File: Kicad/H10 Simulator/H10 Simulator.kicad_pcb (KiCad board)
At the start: 4 copper layers, 54 x 35.2 mm, 15 parts, among them J1 To Controller, J2 H10 ReaderPunch, J3 To Simulator, U1 74xx165, U2 74xx595, U3 74xx04, U4 74xx595, U5 74xx165, U6 74xx04

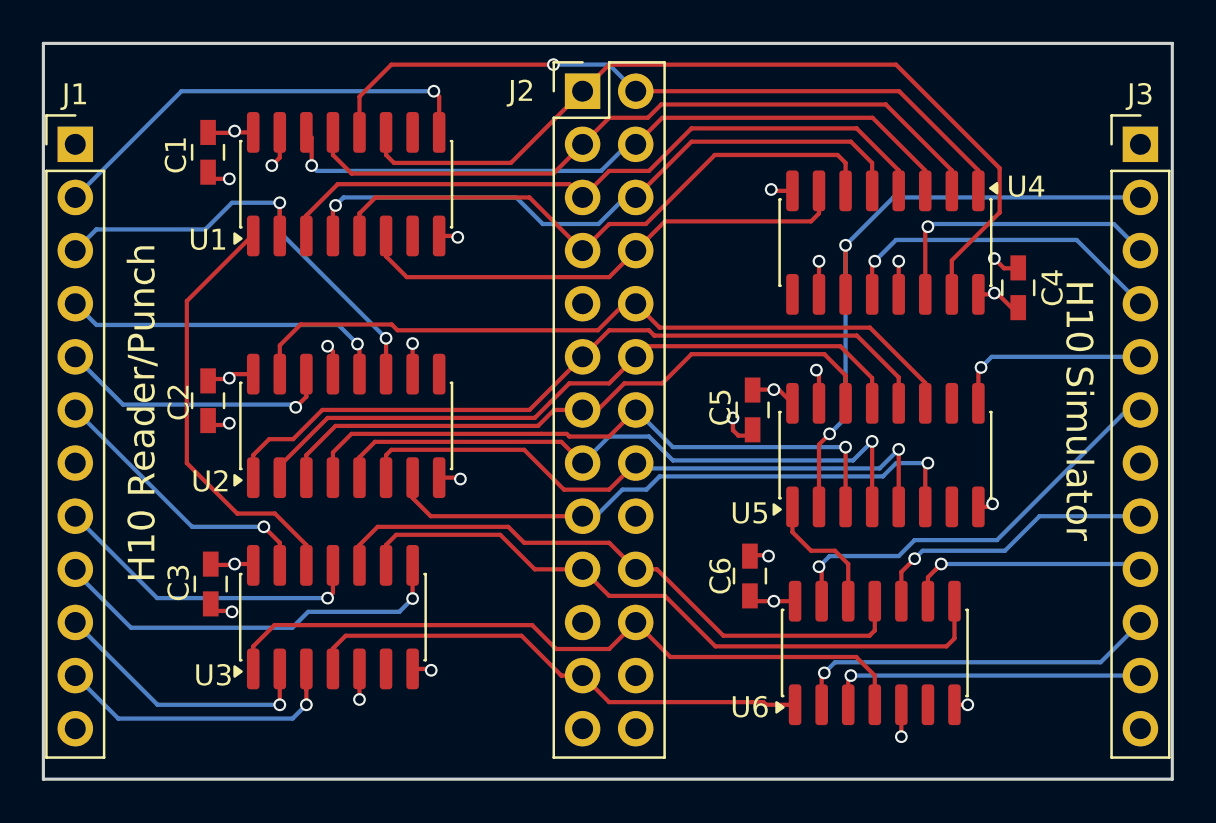
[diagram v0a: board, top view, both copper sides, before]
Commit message: Flip J1 and J3 to back of board, add labels to J2, bump to v0.2
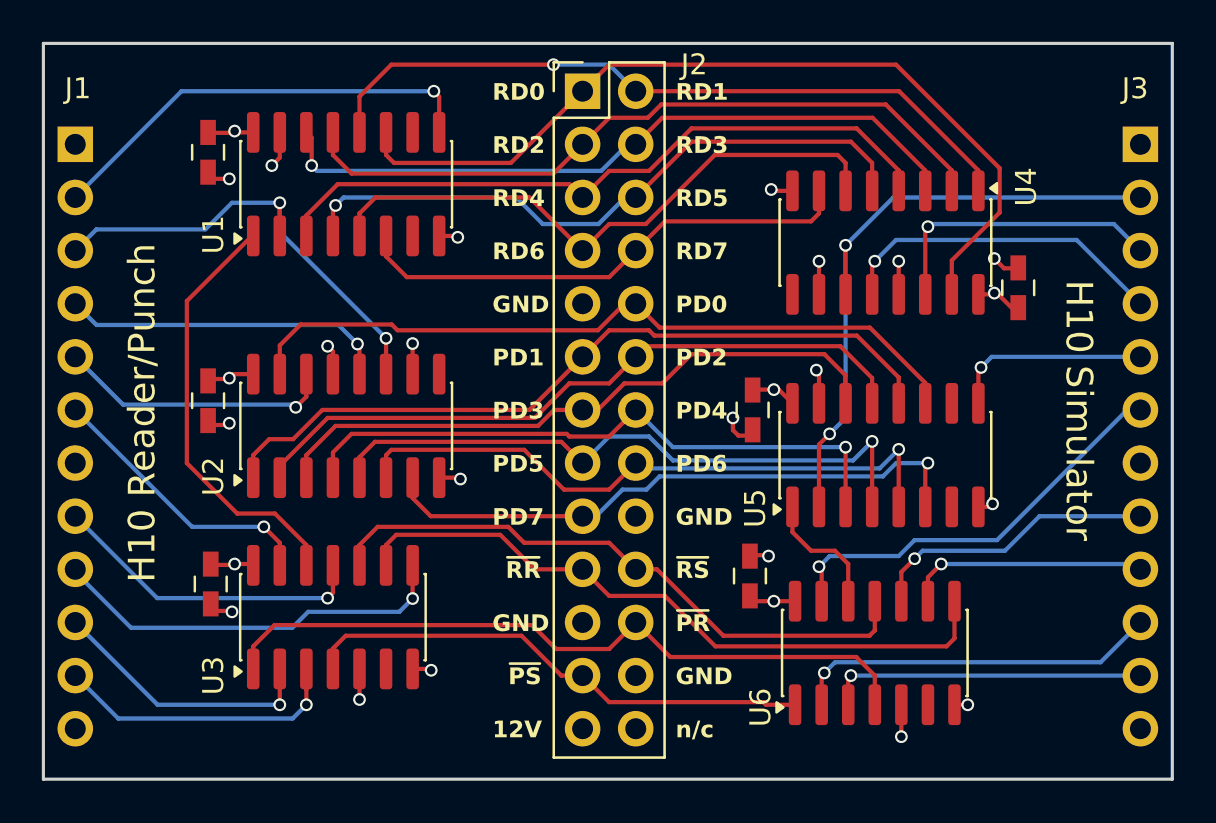
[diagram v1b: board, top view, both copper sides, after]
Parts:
- J1, J3: moved to B.Cu
- turned J1 to 180 degrees
- turned J3 to 180 degrees
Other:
- board text added: "12V"
- board text added: "GND"
- board text added: "PD0"
- board text added: "PD1"
- board text added: "PD2"
- board text added: "PD3"
- board text added: "PD4"
- board text added: "PD5"
- board text added: "PD6"
- board text added: "PD7"
- board text added: "RD0"
- board text added: "RD1"
- board text added: "RD2"
- board text added: "RD3"
- board text added: "RD4"
- board text added: "RD5"
- board text added: "RD6"
- board text added: "RD7"
- board text added: "n/c"
- board text added: "~{PR}"
- board text added: "~{PS}"
- board text added: "~{RR}"
- board text added: "~{RS}"
